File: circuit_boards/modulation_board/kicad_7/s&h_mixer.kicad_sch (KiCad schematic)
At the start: 18 parts

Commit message: Progress on circuit boards
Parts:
- removed U? (x2): TL072, Package_SO:SO-8_5.3x6.2mm_P1.27mm, symbol Amplifier_Operational:TL072
- added U16 (x2): TL072, Package_SO:SOIC-8_3.9x4.9mm_P1.27mm, symbol Amplifier_Operational:TL072
- C901, C902: renamed from C?; footprint Capacitor_SMD:C_0805_2012Metric -> Capacitor_SMD:C_0603_1608Metric
- C903: renamed from C?; value ? -> 100p; footprint Capacitor_SMD:C_0805_2012Metric -> Capacitor_SMD:C_0603_1608Metric
- R901, R902, R904, R905, R906, R907, R908, R909: renamed from R?; footprint Resistor_SMD:R_0805_2012Metric -> Resistor_SMD:R_0603_1608Metric
- R903: renamed from R?; value 47k -> 22k; footprint Resistor_SMD:R_0805_2012Metric -> Resistor_SMD:R_0603_1608Metric
- U15: renamed from U?; footprint (none) -> Package_SO:SOIC-8_3.9x4.9mm_P1.27mm
- gave numbers to parts that had none: 3
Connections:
- net -5V_REF renamed -5V
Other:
- moved on the sheet: C903, R906, R907, R909, U15A

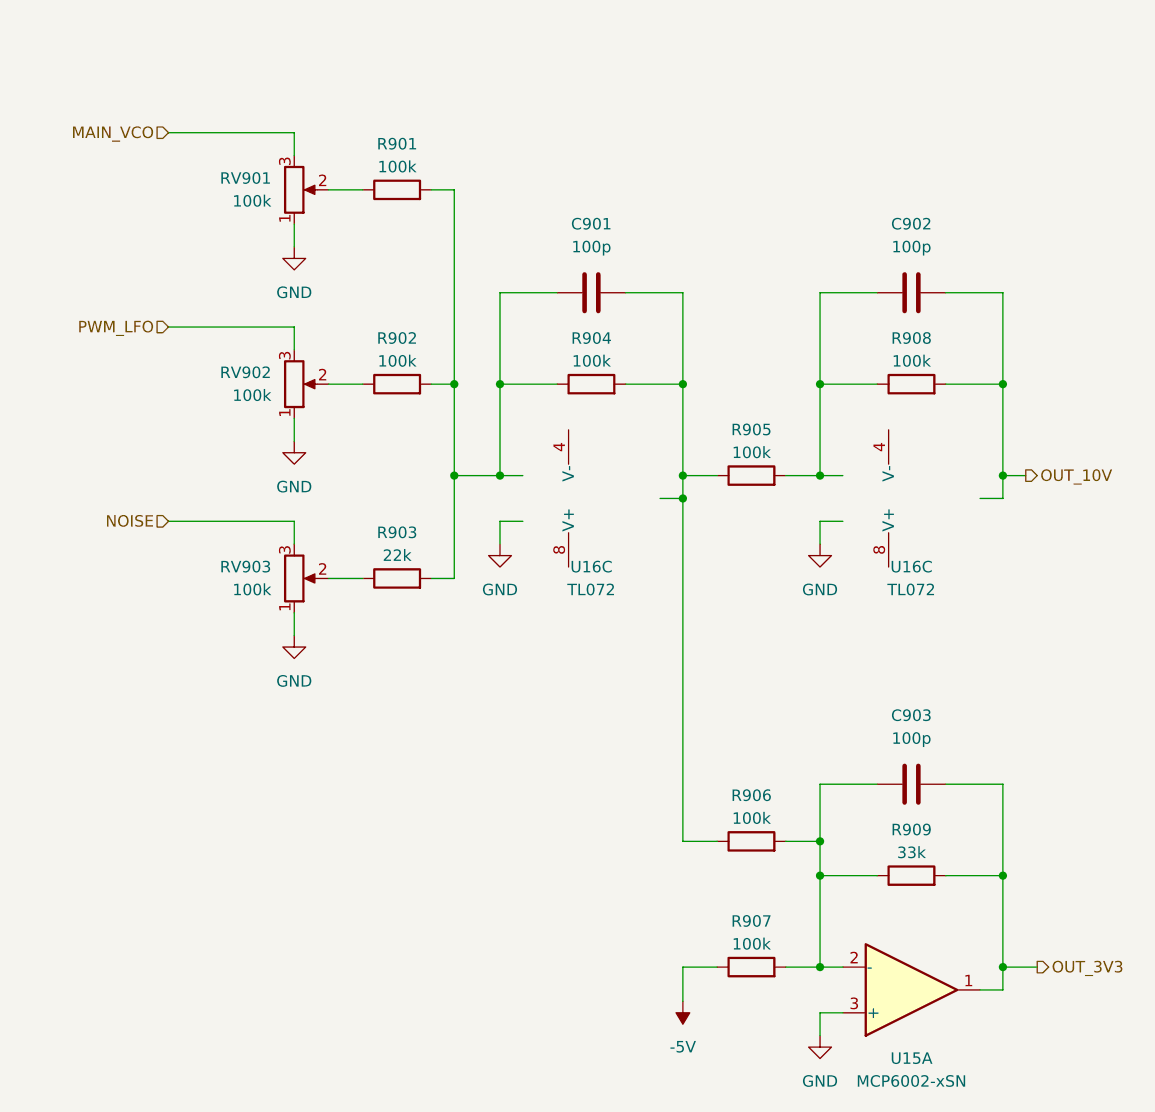
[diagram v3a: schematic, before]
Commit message: Update PCBs, tweak vals, add VCF CV from DAC
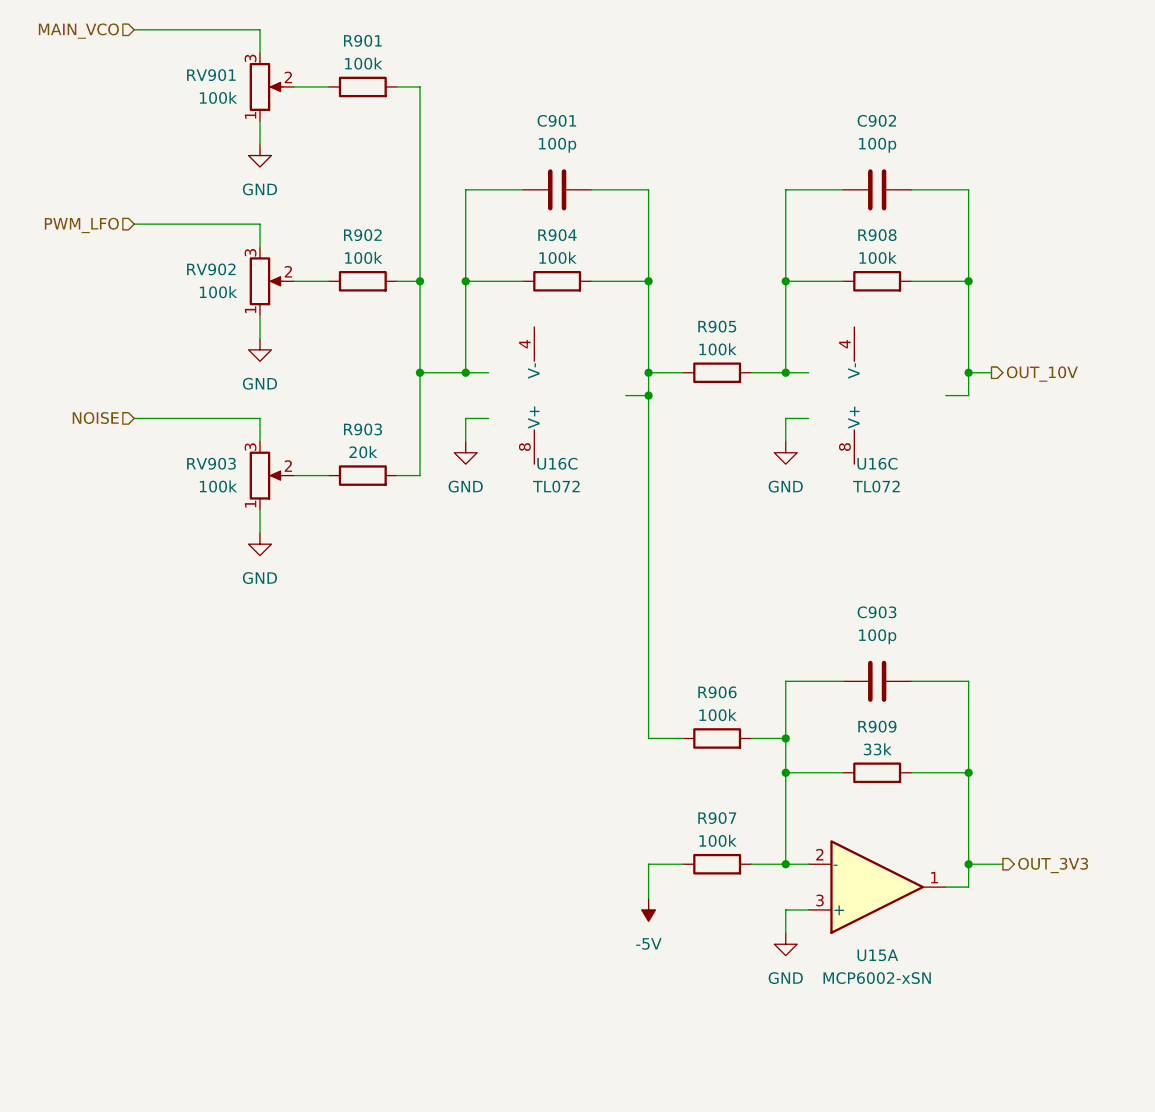
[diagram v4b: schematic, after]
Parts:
- R903: value 22k -> 20k
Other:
- moved on the sheet: C901, C902, C903, R901, R902, R903, R904, R905, R906, R907, R908, R909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

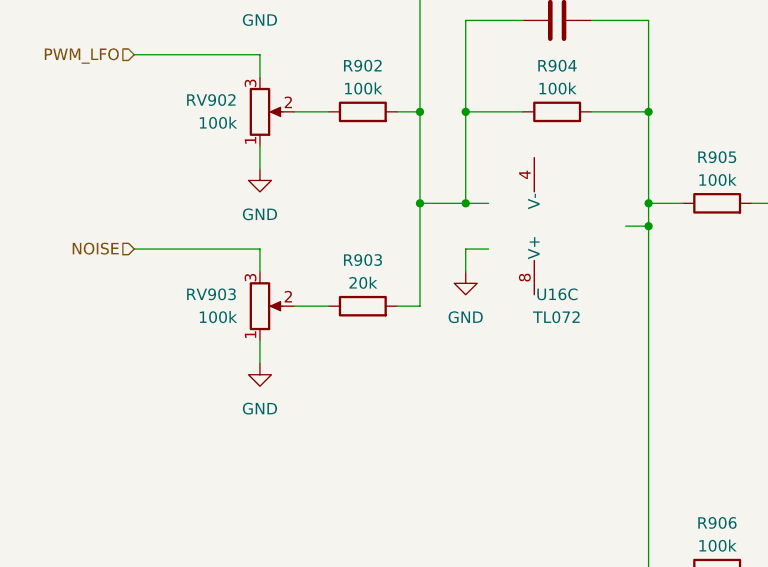
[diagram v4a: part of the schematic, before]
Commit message: Resistor tweaks while evaluating 1st build
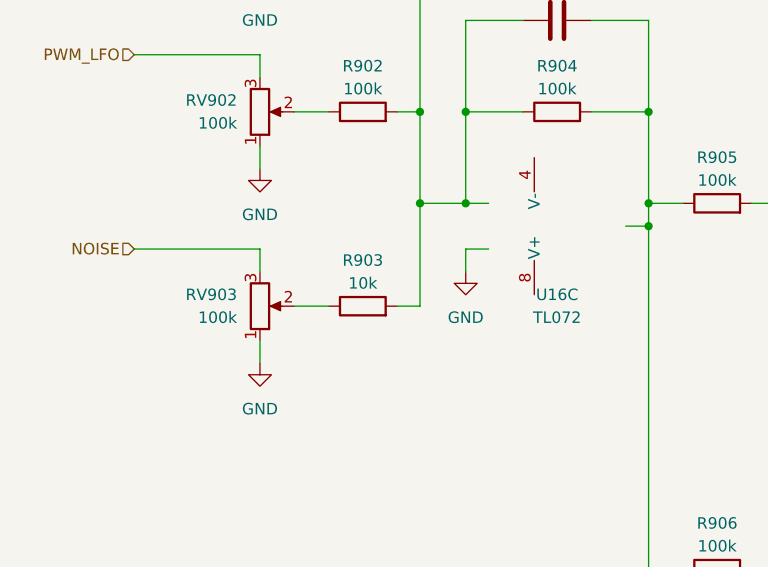
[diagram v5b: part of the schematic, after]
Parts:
- R903: value 20k -> 10k
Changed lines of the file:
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@@
       (effects (font (size 1.27 1.27)))
     )
-    (property "Value" "20k" (at 111.76 91.44 90)
+    (property "Value" "10k" (at 111.76 91.44 90)
       (effects (font (size 1.27 1.27)))
     )

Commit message: Add potentiometer 3d model to VCO and MOD boards
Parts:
- RV901, RV902, RV903: footprint Potentiometer_THT:Potentiometer_Alpha_RD901F-40-00D_Single_Vertical -> custom_footprints:Potentiometer_Alpha_RD901F-40-00D_Single_Vertical
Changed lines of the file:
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@@
       (effects (font (size 1.27 1.27)) (justify right))
     )
-    (property "Footprint" "Potentiometer_THT:Potentiometer_Alpha_RD901F-40-00D_Single_Vertical" (at 100.33 93.98 0)
+    (property "Footprint" "custom_footprints:Potentiometer_Alpha_RD901F-40-00D_Single_Vertical" (at 100.33 93.98 0)
       (effects (font (size 1.27 1.27)) hide)
     )
@@
       (effects (font (size 1.27 1.27)) (justify right))
     )
-    (property "Footprint" "Potentiometer_THT:Potentiometer_Alpha_RD901F-40-00D_Single_Vertical" (at 100.33 72.39 0)
+    (property "Footprint" "custom_footprints:Potentiometer_Alpha_RD901F-40-00D_Single_Vertical" (at 100.33 72.39 0)
       (effects (font (size 1.27 1.27)) hide)
     )
@@
       (effects (font (size 1.27 1.27)) (justify right))
     )
-    (property "Footprint" "Potentiometer_THT:Potentiometer_Alpha_RD901F-40-00D_Single_Vertical" (at 100.33 50.8 0)
-      (effects (font (size 1.27 1.27)) hide)
-    )
+    (property "Footprint" "custom_footprints:Potentiometer_Alpha_RD901F-40-00D_Single_Vertical" (at 100.33 50.8 0)
+      (effects (font (size 1.27 1.27)) hide)
+    )
